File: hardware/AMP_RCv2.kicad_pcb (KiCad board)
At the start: 2 copper layers, 100 x 85 mm, 45 parts, among them J1 USB_C_Receptacle_USB2.0_16P, SW1 SW_UP, SW2 SW_LEFT, SW3 SW_DOWN, SW4 SW_RIGHT, SW5 ON/OFF, U1 TLV61070ADB, U2 MCP73831-2-OT, U3 JOYSTICK_LEFT, U4 JOYSTICK_RIGHT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

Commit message: Finishing touches
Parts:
- added G***: LOGO, AMP_Custom:Logo, B.Cu at (146.5, 119.2)
- J1: footprint AMP_Custom:USB_C_Receptacle_Amphenol_C12402012 -> Connector_USB:USB_C_Receptacle_GCT_USB4085
- moved J1 6.27 mm to (108.7, 113.0)
- moved R13 2.42 mm to (112.5, 114.1)
- moved R12 2.39 mm to (112.5, 116.2)
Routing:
- net VBUS: track 38.4 -> 25.3 mm
- net Net-(J1-CC2): track 2.21 -> 14.8 mm, vias 0 -> 2
- net GND: track 43.7 -> 47.4 mm
- net Net-(J1-CC1): track 2.00 -> 3.03 mm
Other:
- board text added: "AMP RCv2 Revision B"

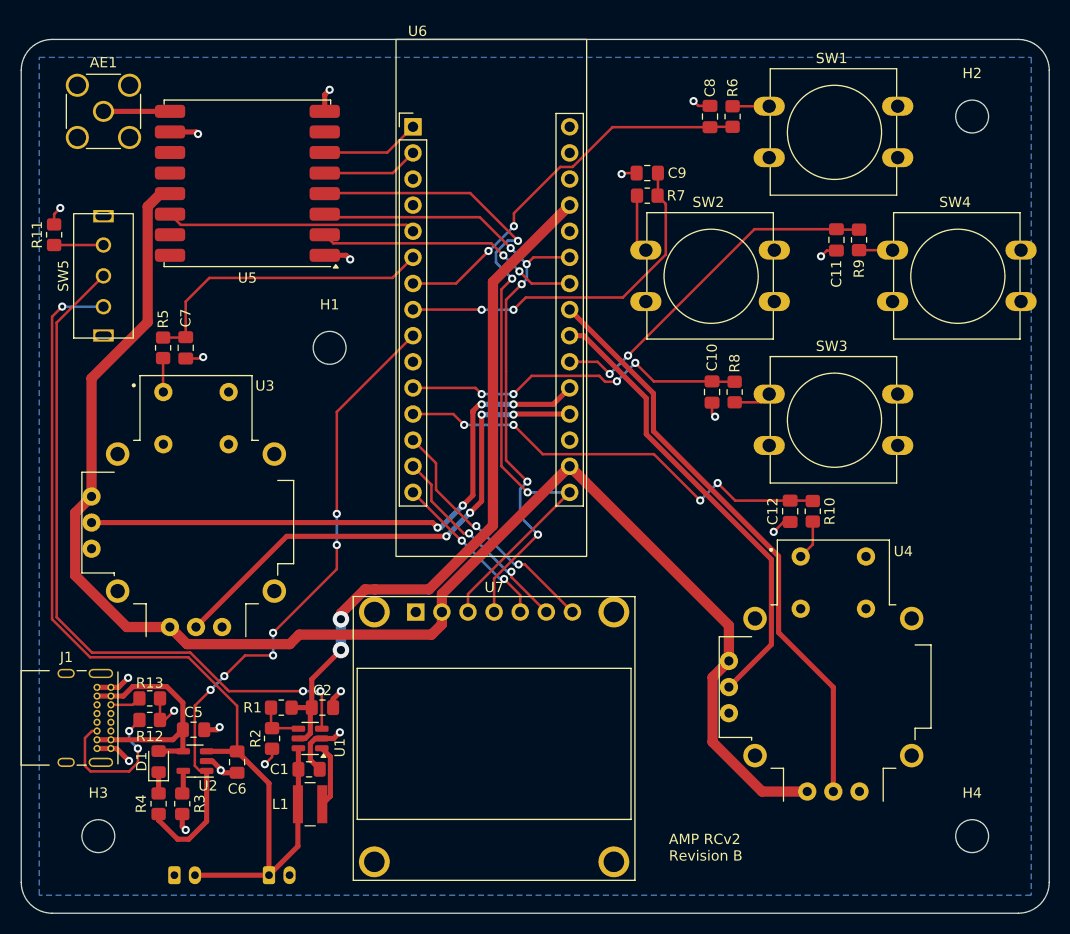
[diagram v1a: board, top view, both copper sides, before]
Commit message: Change text size
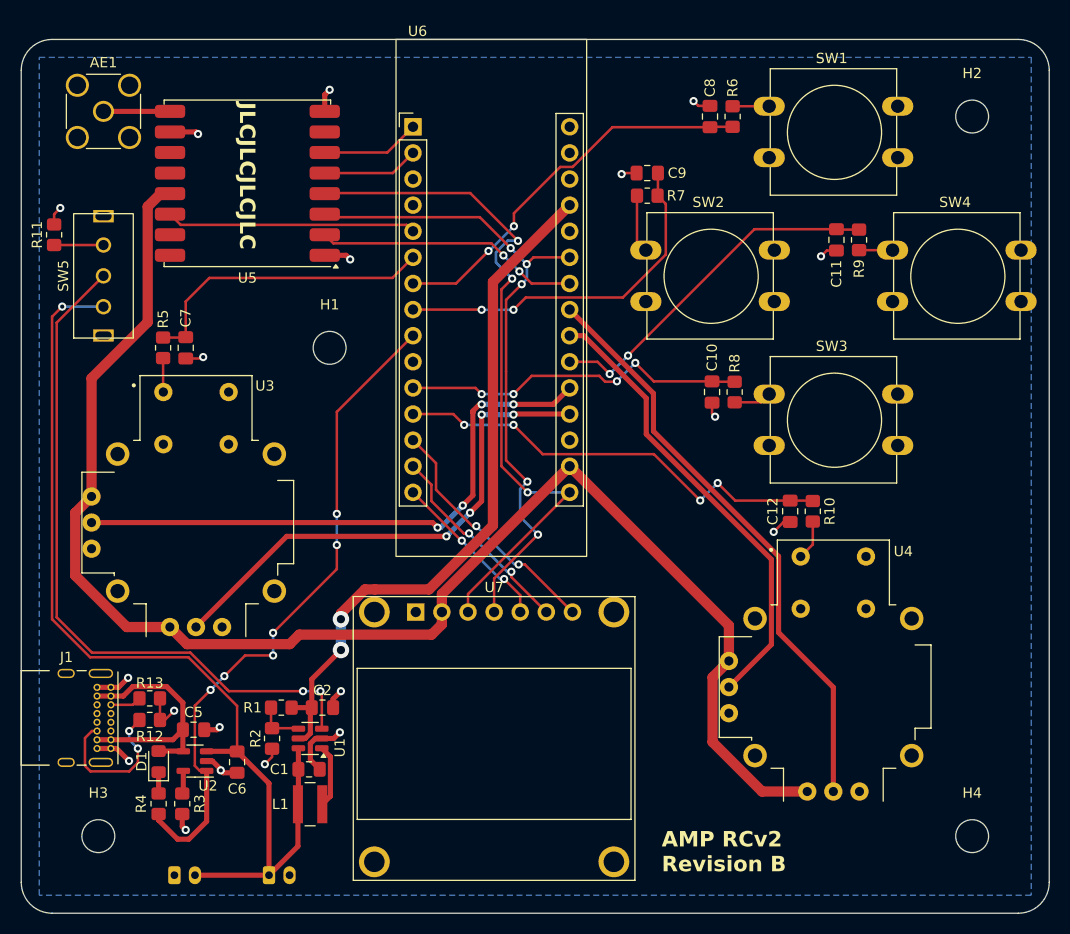
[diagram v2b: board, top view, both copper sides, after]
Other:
- board text added: "JLCJLCJLCJLC"
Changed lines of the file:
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@@
 	)
 	(gr_text "AMP RCv2\nRevision B"
-		(at 163 130 0)
+		(at 162.3 131.1 0)
 		(layer "F.SilkS")
 		(effects
 			(font
-				(size 1 1)
-				(thickness 0.15)
+				(size 1.5 1.5)
+				(thickness 0.3)
+				(bold yes)
 			)
 			(justify left bottom)
+		)
+	)
+	(gr_text "JLCJLCJLCJLC"
+		(at 121.1 56.1 270)
+		(layer "F.SilkS")
+		(effects
+			(font
+				(size 1.5 1.5)
+				(thickness 0.3)
+				(bold yes)
+			)
+			(justify left bottom)
